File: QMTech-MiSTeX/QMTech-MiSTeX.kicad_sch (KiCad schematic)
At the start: 31 parts, among them J1 RPi_GPIO, J12 Conn_01x03_Pin, J13 USB_C_Receptacle_USB2.0, J2 MiSTer SDRAM Module, J3 USB_C_Receptacle_USB2.0, J4 Conn_02x32_Odd_Even, J5 Conn_02x32_Odd_Even, J6 Conn_01x06_Pin, J7 Conn_01x03_Pin, J8 Conn_01x03_Pin, SW5 TK-6580S-1

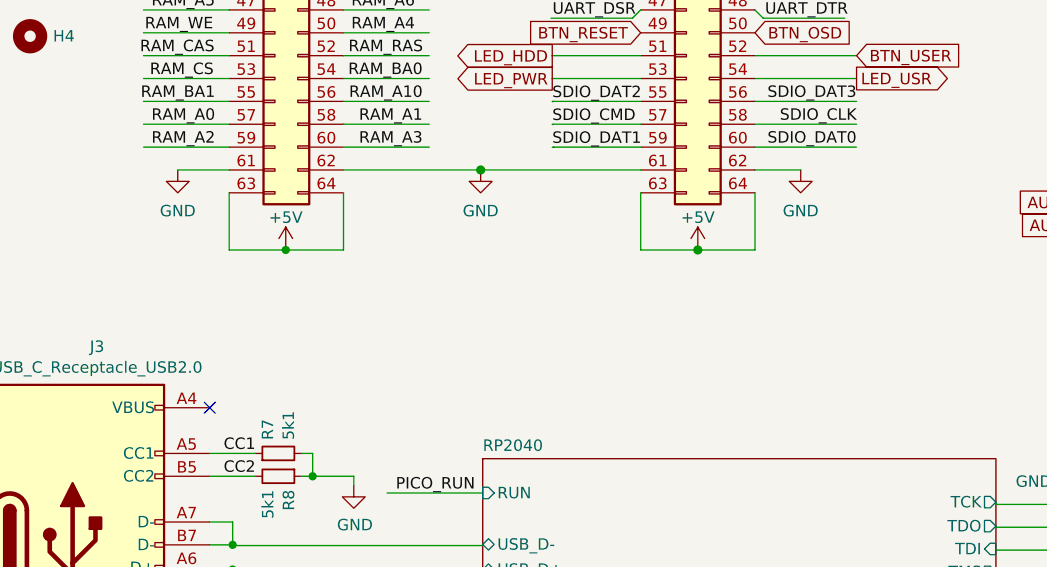
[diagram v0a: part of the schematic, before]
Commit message: QMTech-MiSTeX: OSHW logo on front mask, add instructions for installing SDRAM
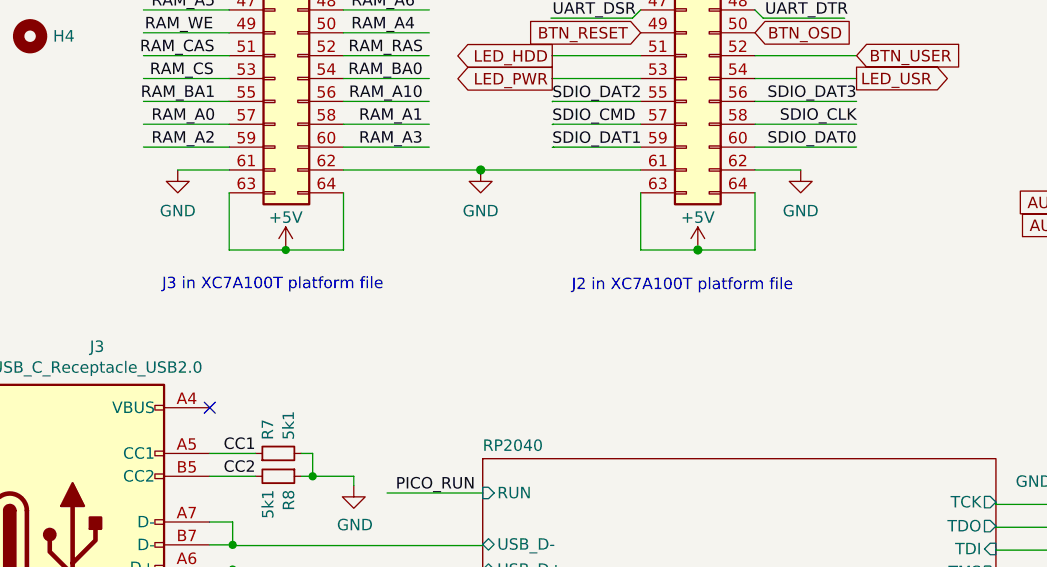
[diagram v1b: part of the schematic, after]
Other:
- note added: "J2 in XC7A100T platform file"
- note added: "J3 in XC7A100T platform file"
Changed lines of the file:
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@@
     )
+  )
+  (text "J3 in XC7A100T platform file" (at 116.1034 108.7628 0)
+    (effects (font (size 1.27 1.27)) (justify left bottom))
+  )
+  (text "J2 in XC7A100T platform file" (at 161.6202 108.8644 0)
+    (effects (font (size 1.27 1.27)) (justify left bottom))
   )
   (label "RAM_DQ13" (at 59.5333 103.0732 180) (fields_autoplaced)

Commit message: QMTech-MiSTeX WIP
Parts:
- removed R1, R3: 0R, R_0402_1005Metric, symbol jlcpcb-basic-resistor-0402:0R
- removed R2, R4: DNP, R_0402_1005Metric, symbol jlcpcb-basic-resistor-0402:0R
- added C45: 10u, Capacitor_SMD:C_0603_1608Metric, symbol Device:C_Small
- added C46, C47: 100uF, easyeda2kicad:C1206, symbol easyeda2kicad:CL31A107MQHNNNE
- added L5: 10uH, easyeda2kicad:L0805, symbol easyeda2kicad:SDFL2012S100KTF
- added R1, R3: 0R, R_0805_2012Metric, symbol jlcpcb-basic-resistor-0805:0R
- added R2, R4: DNP, R_0805_2012Metric, symbol jlcpcb-basic-resistor-0805:0R
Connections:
- net +3V3: now also L5.1
- net +5V: now also R1.1
- net GND: now also C45.2, C46.2, C47.2, R2.2, R4.2
- net at J2.29 (Pin_29): now also C45.1, C46.1, R3.2, R4.1
- net at J2.11 (Pin_11): now also C47.1, R1.2, R2.1
- new net: L5.2, R3.1

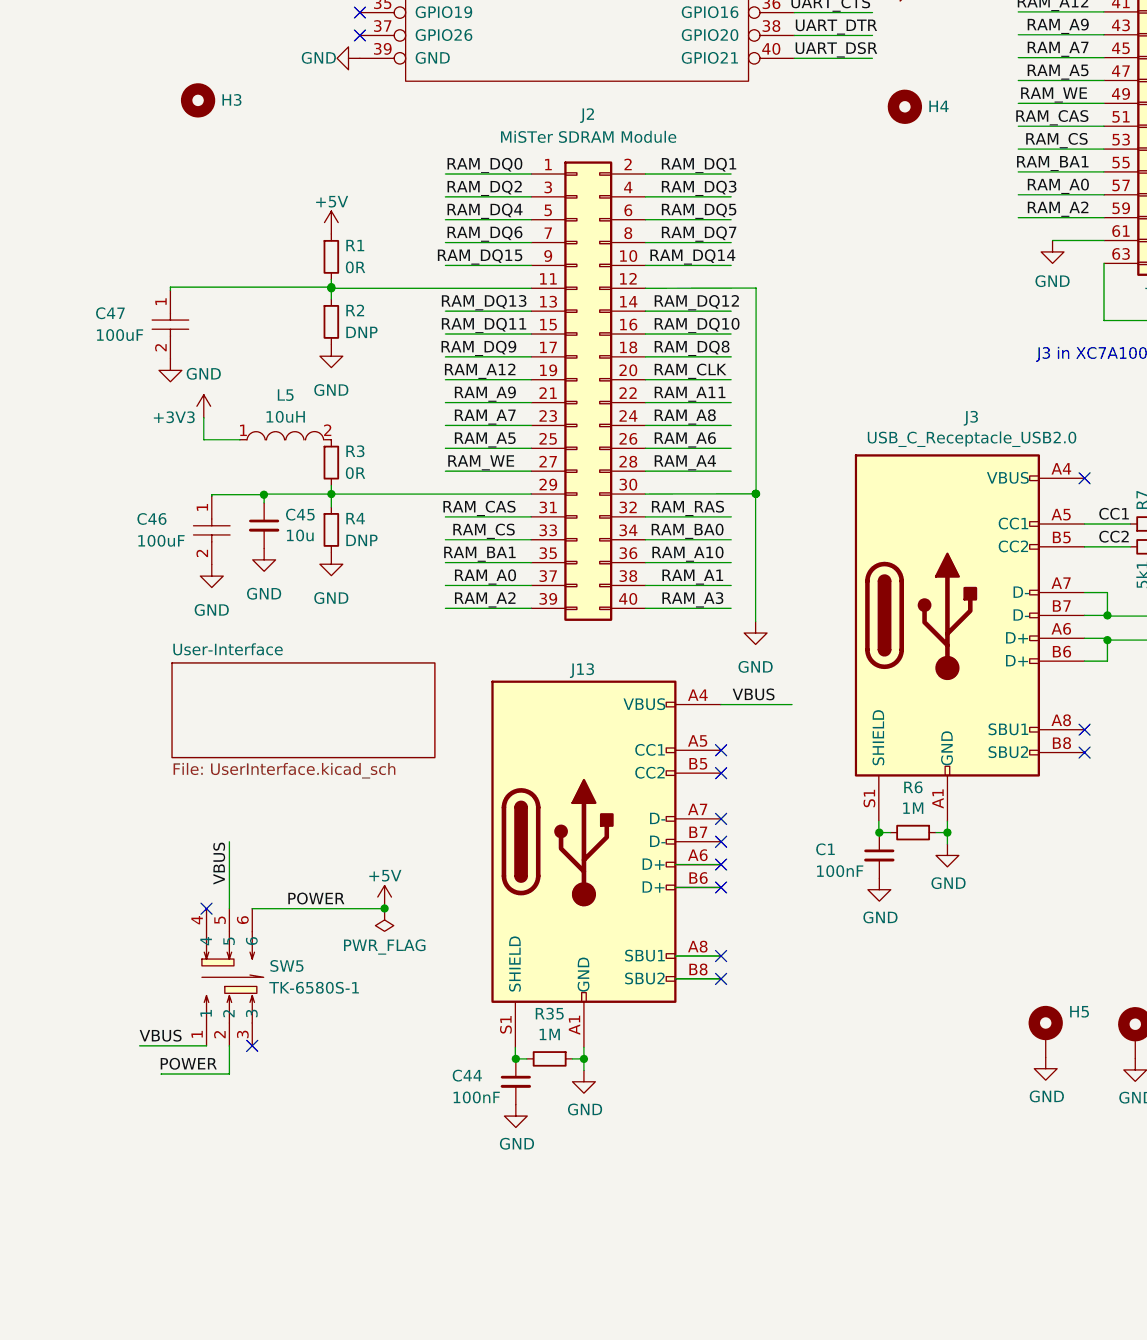
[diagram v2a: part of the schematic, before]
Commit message: power filtering, testpoints, bottom caps, more decoupling, teardrops
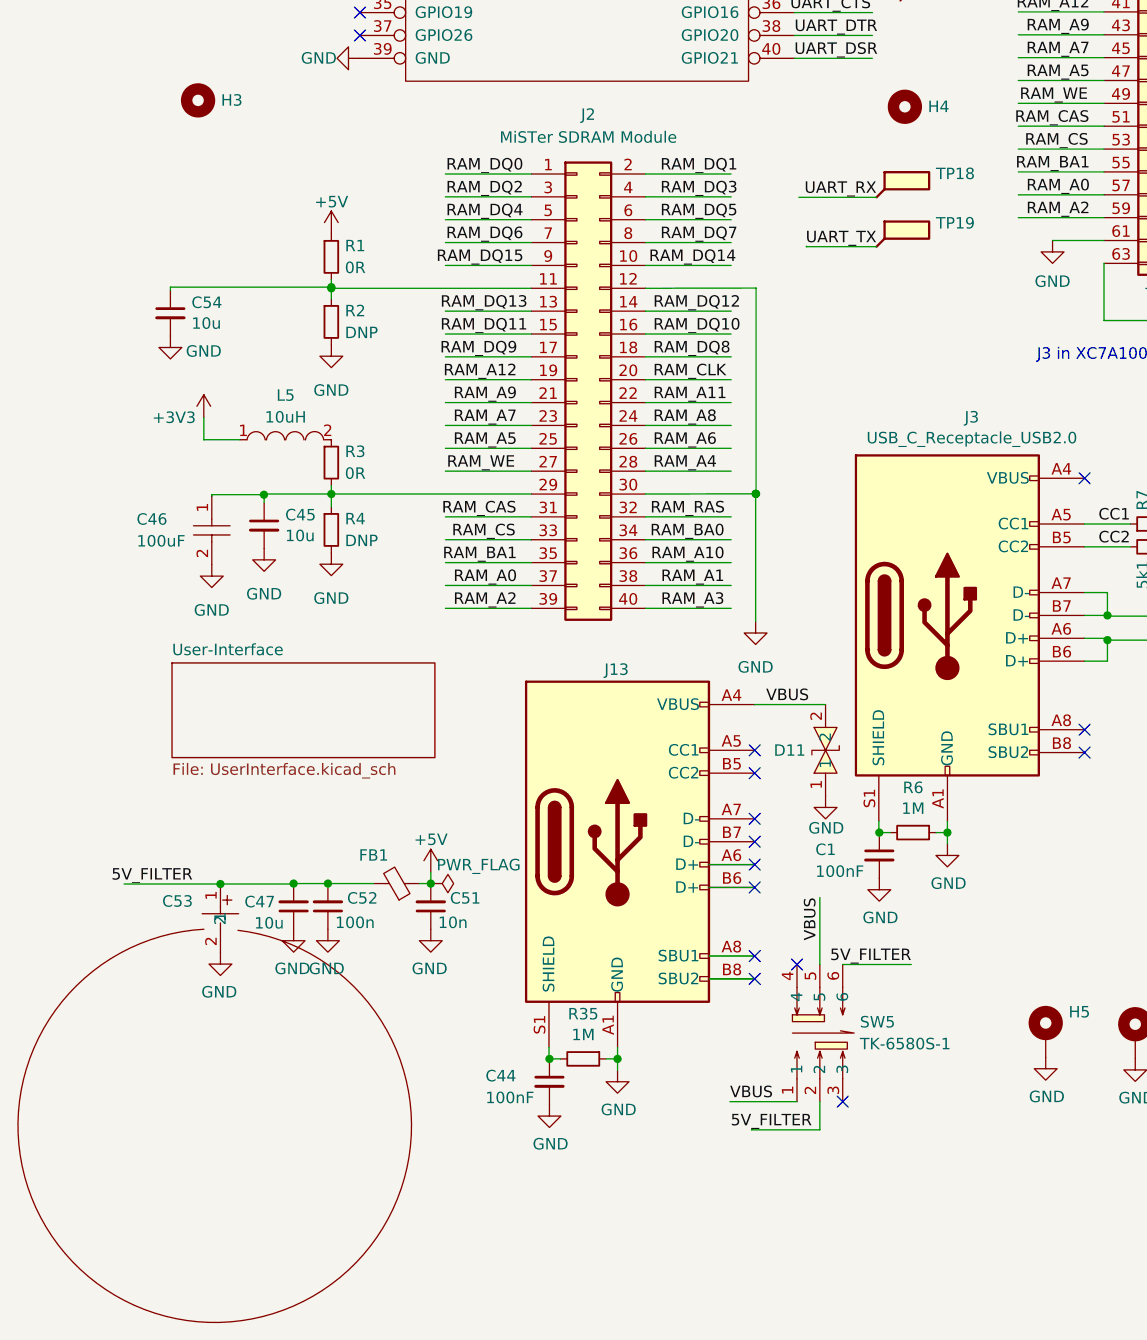
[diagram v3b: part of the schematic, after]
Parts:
- removed C47: 100uF, easyeda2kicad:C1206, symbol easyeda2kicad:CL31A107MQHNNNE
- added C47: UWX1C101MCL1GB, easyeda2kicad:CAP-SMD_BD6.3-L6.6-W6.6-FD, symbol easyeda2kicad:UWX1C101MCL1GB
- added C51: 10n, Capacitor_SMD:C_0805_2012Metric, symbol Device:C_Small
- added C52: 100n, Capacitor_SMD:C_0603_1608Metric, symbol Device:C_Small
- added C53: 10u, Capacitor_SMD:C_0805_2012Metric, symbol Device:C_Small
- added C54: 10u, Capacitor_SMD:C_0603_1608Metric, symbol Device:C_Small
- added D11: P6SMB6.8CA-C78395, easyeda2kicad:SMB_L4.6-W3.6-LS5.3-BI, symbol easyeda2kicad:P6SMB6.8CA-C78395
- added FB1: 1.5A, Inductor_SMD:L_1206_3216Metric, symbol Device:Ferrite_Bead_Small
- added TP18, TP19: TestPoint_Flag, TestPoint:TestPoint_Pad_D1.5mm, symbol Connector:TestPoint_Flag
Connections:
- net +5V: now also C51.2, FB1.1; no longer SW5.2, SW5.6
- net GND: now also C47.2, C51.1, C52.1, C53.1, C54.2, D11.1
- net UART_RX: now also TP18.1
- net UART_TX: now also TP19.1
- net VBUS: now also D11.2
- net at J2.11 (Pin_11), R1.2, R2.1: now also C54.1
- new net 5V_FILTER: C47.1, C52.2, C53.2, FB1.2, SW5.2, SW5.6
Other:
- moved on the sheet: C44, J13, R35, SW5

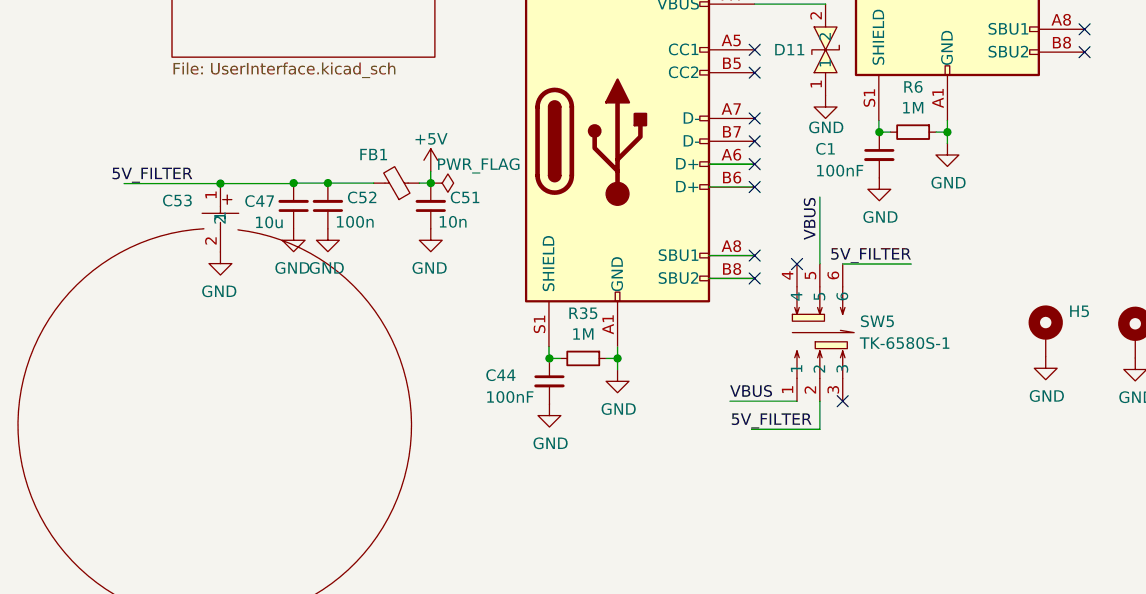
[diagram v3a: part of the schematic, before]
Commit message: remove power switch because of bad quality, add BOM/CPL
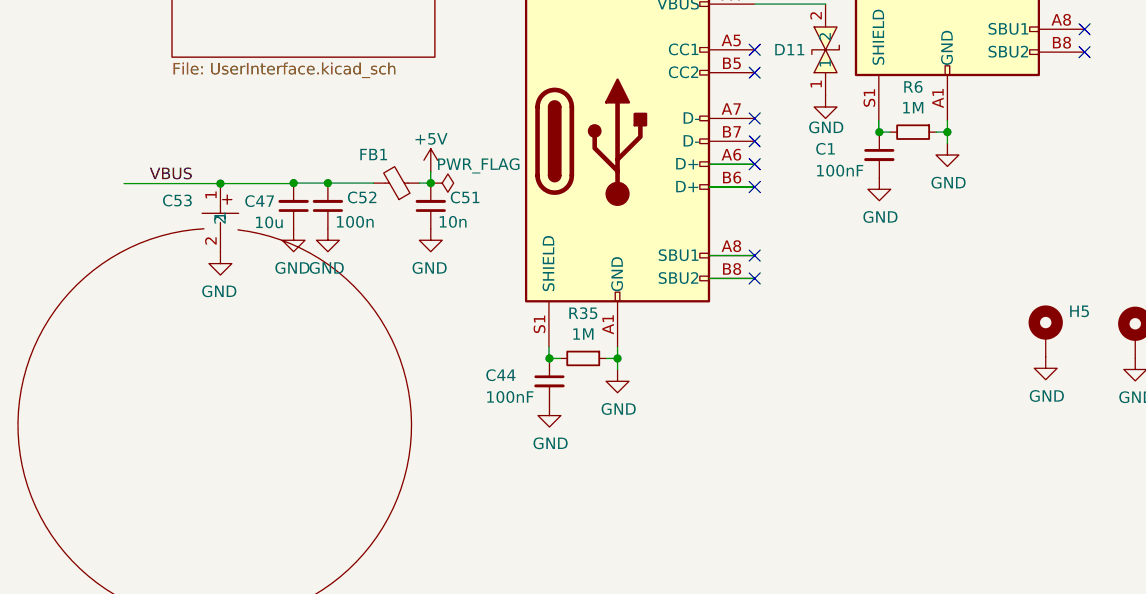
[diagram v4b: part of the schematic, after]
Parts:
- removed SW5: TK-6580S-1, easyeda2kicad:SW-SMD_TK-6580S-1, symbol easyeda2kicad:TK-6580S-1
- FB1: value 1.5A -> 6A; LCSC C16902 -> C337884
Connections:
- net 5V_FILTER is gone; now on net VBUS: C47.1, C52.2, C53.2, FB1.2
- no-connect marks 25 -> 23
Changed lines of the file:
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@@
   (no_connect (at 84.7598 154.4066))
   (no_connect (at 84.7598 151.8666))
-  (no_connect (at 94.5388 190.9064))
   (no_connect (at 84.7598 164.5666))
   (no_connect (at 40.894 26.7208))
@@
   (no_connect (at 84.7598 167.1066))
   (no_connect (at 121.412 121.6406))
-  (no_connect (at 89.4588 175.6664))
   (no_connect (at 40.894 72.4408))
   (no_connect (at 40.894 69.9008))
@@
     (stroke (width 0) (type default))
   )
-  (wire (pts (xy 91.9988 190.9064) (xy 91.9988 194.0306))
-    (stroke (width 0) (type default))
-  )
   (wire (pts (xy 37.719 123.3932) (xy 59.9186 123.3932))
     (stroke (width 0) (type default))
@@
     (stroke (width 0) (type default))
   )
-  (wire (pts (xy 91.9988 168.2242) (xy 91.9988 175.6664))
-    (stroke (width 0) (type default))
-  )
   (wire (pts (xy 151.511 95.2246) (xy 169.291 95.2246))
     (stroke (width 0) (type solid))
@@
     (stroke (width 0) (type default))
   )
-  (wire (pts (xy 84.4275 194.0306) (xy 84.4275 194.043))
-    (stroke (width 0) (type default))
-  )
   (wire (pts (xy 228.2952 144.145) (xy 228.2952 151.765))
     (stroke (width 0) (type default))
@@
     (stroke (width 0) (type default))
   )
-  (wire (pts (xy 84.4275 194.0306) (xy 91.9988 194.0306))
-    (stroke (width 0) (type default))
-  )
   (wire (pts (xy 208.7626 142.5448) (xy 208.7626 142.494))
     (stroke (width 0) (type default))
@@
     (stroke (width 0) (type default))
   )
-  (wire (pts (xy 102.1588 175.6664) (xy 94.5388 175.6664))
-    (stroke (width 0) (type default))
-  )
   (wire (pts (xy 59.9186 97.9932) (xy 50.3936 97.9932))
     (stroke (width 0) (type default))
@@
     (stroke (width 0) (type default))
   )
-  (wire (pts (xy 82.0166 190.9064) (xy 89.4588 190.9064))
-    (stroke (width 0) (type default))
-  )
   (wire (pts (xy 169.291 21.5646) (xy 168.656 21.5646))
     (stroke (width 0) (type default))
@@
     (effects (font (size 1.27 1.27)) (justify right bottom))
   )
-  (label "5V_FILTER" (at 22.31 166.7289 180) (fields_autoplaced)
+  (label "VBUS" (at 22.31 166.7289 180) (fields_autoplaced)
     (effects (font (size 1.27 1.27)) (justify right bottom))
   )
@@
     (effects (font (size 1.27 1.27)) (justify right bottom))
   )
-  (label "5V_FILTER" (at 91.1146 194.0306 180) (fields_autoplaced)
-    (effects (font (size 1.27 1.27)) (justify right bottom))
-  )
   (label "RAM_DQ9" (at 122.0427 67.2846 180) (fields_autoplaced)
     (effects (font (size 1.27 1.27)) (justify right bottom))
@@
     (effects (font (size 1.27 1.27)) (justify left bottom))
   )
-  (label "5V_FILTER" (at 102.1588 175.6664 180) (fields_autoplaced)
-    (effects (font (size 1.27 1.27)) (justify right bottom))
-  )
   (label "RAM_DQ1" (at 74.2739 87.8332 0) (fields_autoplaced)
     (effects (font (size 1.27 1.27)) (justify left bottom))
@@
     (effects (font (size 1.27 1.27)) (justify left bottom))
   )
-  (label "VBUS" (at 91.9988 168.2242 270) (fields_autoplaced)
-    (effects (font (size 1.27 1.27)) (justify right bottom))
-  )
   (label "RAM_A4" (at 73.4799 120.8532 0) (fields_autoplaced)
     (effects (font (size 1.27 1.27)) (justify left bottom))
@@
     (effects (font (size 1.27 1.27)) (justify right bottom))
   )
-  (label "VBUS" (at 82.0166 190.9064 0) (fields_autoplaced)
-    (effects (font (size 1.27 1.27)) (justify left bottom))
-  )
   (label "RAM_A8" (at 137.1323 74.9046 0) (fields_autoplaced)
     (effects (font (size 1.27 1.27)) (justify left bottom))
@@
     )
   )
-  (symbol (lib_id "easyeda2kicad:TK-6580S-1") (at 91.9988 183.2864 0) (unit 1)
-    (in_bom yes) (on_board yes) (dnp no) (fields_autoplaced)
-    (property "Reference" "SW5" (at 96.4438 182.0743 0)
-      (effects (font (size 1.27 1.27)) (justify left))
-    )
-    (property "Value" "TK-6580S-1" (at 96.4438 184.4985 0)
-      (effects (font (size 1.27 1.27)) (justify left))
-    )
-    (property "Footprint" "easyeda2kicad:SW-SMD_TK-6580S-1" (at 91.9988 198.5264 0)
-      (effects (font (size 1.27 1.27)) hide)
-    )
-    (property "Datasheet" "" (at 91.9988 183.2864 0)
-      (effects (font (size 1.27 1.27)) hide)
-    )
-    (property "LCSC Part" "C528774" (at 91.9988 201.0664 0)
-      (effects (font (size 1.27 1.27)) hide)
-    )
-    (pin "2")
-    (pin "4")
-    (pin "6")
-    (pin "5")
-    (pin "1")
-    (pin "3")
-    (instances
-      (project "QMTech-MiSTeX"
-        (path "/bf95850e-2fcb-4784-a603-f17fc357556b"
-          (reference "SW5") (unit 1)
-        )
-      )
-    )
-  )
   (symbol (lib_id "Connector:TestPoint_Flag") (at 98.298 90.424 0) (unit 1)
     (in_bom yes) (on_board yes) (dnp no) (fields_autoplaced)
@@
       (effects (font (size 1.27 1.27)))
     )
-    (property "Value" "1.5A" (at 44.958 163.7815 90)
+    (property "Value" "6A" (at 44.958 163.7815 90)
       (effects (font (size 1.27 1.27)) hide)
     )
@@
       (effects (font (size 1.27 1.27)) hide)
     )
-    (property "LCSC" "C16902" (at 44.958 166.6748 90)
+    (property "LCSC" "C337884" (at 44.958 166.6748 90)
       (effects (font (size 1.27 1.27)) hide)
     )
